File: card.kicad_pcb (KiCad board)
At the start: 2 copper layers, 89 x 51 mm, 21 parts, among them J1 Conn_01x08, J2 Conn_01x04, J3 Conn_01x04, U1 ISP1907, U2 MTCH6102

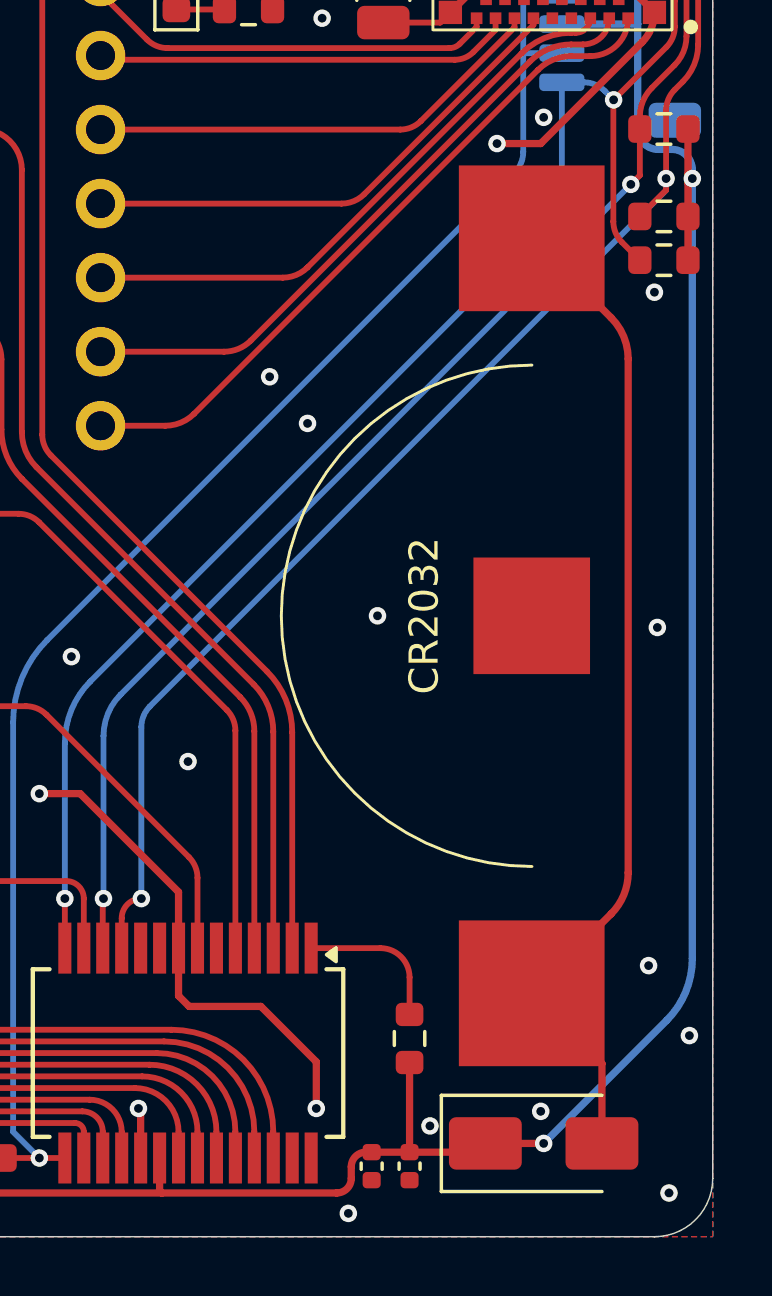
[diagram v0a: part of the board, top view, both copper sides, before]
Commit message: add switch
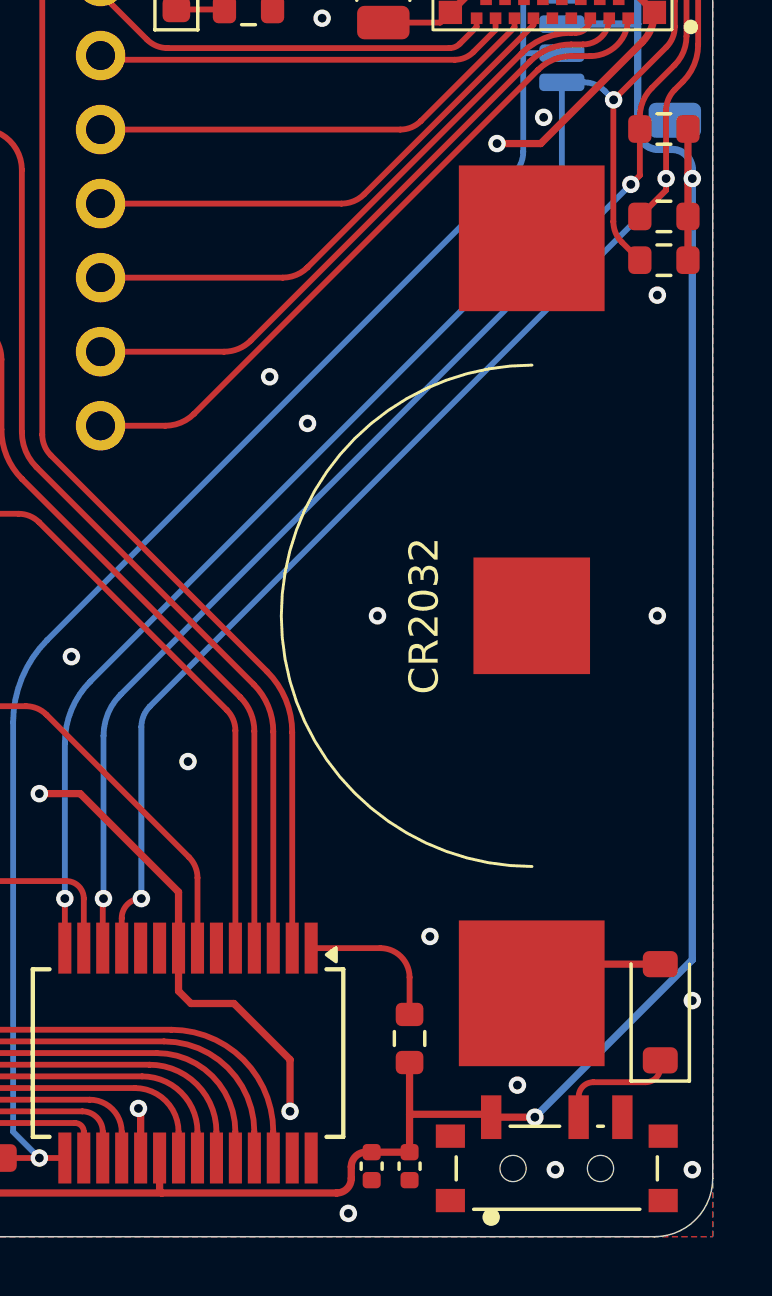
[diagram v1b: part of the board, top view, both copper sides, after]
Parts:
- added SW1: SW_SPDT, Button_Switch_SMD:SW_SPDT_PCM12, F.Cu at (133.7, 98.3)
- D1: footprint Diode_SMD:D_SMA -> Diode_SMD:D_SOD-123
- moved D1 6.02 mm to (137.2, 93.3), turned to 90 degrees
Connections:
- D1 pad 1: +BATT -> Net-(D1-K)
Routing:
- net Net-(BT1-+): track 34.6 -> 4.82 mm
- net Net-(D1-K): track 0.00 -> 4.28 mm
- net +BATT: track 104.2 -> 103.2 mm
- net GND: track 50.0 -> 49.2 mm
